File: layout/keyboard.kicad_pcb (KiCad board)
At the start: 2 copper layers, 281.5 x 105.2 mm, 127 parts, among them SW1 SW_PUSH, U1 ATMEGA32U4, X1 XTAL_GND

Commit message: switches layout
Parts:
- removed C1, C2, C3, C4, C5, C6, C7: 22pF, Capacitor_SMD:C_0805_2012Metric_Pad1.15x1.40mm_HandSolder
- removed D_A, D_ALT, D_B, D_BKSP, D_BSLSH, D_C, D_CBRAC, D_COMMA, D_CTRL, D_D, D_DOT, D_E, D_EQUAL, D_ESC, D_F, D_G, D_H, D_I, D_J, D_K, D_L, D_M, D_MINUS, D_N, D_O, D_OBRAC, D_P, D_Q, D_QUOTE, D_R, D_S, D_SEMIC, D_SHIFT, D_SLASH, D_SPACE, D_SUPER, D_T, D_TAB, D_U, D_V, D_W, D_X, D_Y, D_Z, D_`: D, keyboard_parts:D_SOD123_axial
- removed K_A, K_B, K_C, K_CBRAC, K_COMMA, K_D, K_DOT, K_E, K_EQUAL, K_ESC, K_F, K_G, K_H, K_I, K_J, K_K, K_L, K_M, K_MINUS, K_N, K_O, K_OBRAC, K_P, K_Q, K_QUOTE, K_R, K_S, K_SEMIC, K_SLASH, K_T, K_U, K_V, K_W, K_X, K_Y, K_Z, K_`: KEYSW, MX_Alps_Hybrid:MX-1U-NoLED
- removed K_ALT, K_SUPER: KEYSW, MX_Alps_Hybrid:MX-1.25U-NoLED
- removed K_BKSP: KEYSW, MX_Alps_Hybrid:MX-2U-NoLED
- removed K_BSLSH, K_TAB: KEYSW, MX_Alps_Hybrid:MX-1.5U-NoLED
- removed K_CTRL: KEYSW, MX_Alps_Hybrid:MX-1.75U-NoLED
- removed K_SHIFT, K_SPACE: KEYSW, MX_Alps_Hybrid:MX-2.25U-NoLED
- removed R1, R2: 10k, Resistor_SMD:R_0805_2012Metric_Pad1.15x1.40mm_HandSolder
- removed R3, R4: 22, Resistor_SMD:R_0805_2012Metric_Pad1.15x1.40mm_HandSolder
- removed SW1: SW_PUSH, Button_Switch_SMD:SW_SPST_TL3342
- removed USB1: Molex-0548190589, keyboard_parts:Molex-0548190589-Assembly
- removed X1: XTAL_GND, Crystal:Crystal_SMD_5032-4Pin_5.0x3.2mm
- added D_A1: D, keyboard_parts:D_SOD123_axial, F.Cu at (57.9, -65.9)
- added D_ALT1: D, keyboard_parts:D_SOD123_axial, F.Cu at (88.9, -27.8)
- added D_B1: D, keyboard_parts:D_SOD123_axial, F.Cu at (134.1, -46.8)
- added D_BKSP1: D, keyboard_parts:D_SOD123_axial, F.Cu at (258.0, -104.0)
- added D_BSLSH1: D, keyboard_parts:D_SOD123_axial, F.Cu at (253.2, -84.9)
- added D_C1: D, keyboard_parts:D_SOD123_axial, F.Cu at (96.0, -46.8)
- added D_CBRAC1: D, keyboard_parts:D_SOD123_axial, F.Cu at (234.2, -27.8)
- added D_COMMA1: D, keyboard_parts:D_SOD123_axial, F.Cu at (191.3, -47.1)
- added D_CTRL1: D, keyboard_parts:D_SOD123_axial, F.Cu at (31.8, -65.9)
- added D_D1: D, keyboard_parts:D_SOD123_axial, F.Cu at (134.1, -65.9)
- added D_DOT1: D, keyboard_parts:D_SOD123_axial, F.Cu at (210.3, -46.8)
- added D_E1: D, keyboard_parts:D_SOD123_axial, F.Cu at (191.3, -65.9)
- added D_EQUAL1: D, keyboard_parts:D_SOD123_axial, F.Cu at (215.1, -27.8)
- added D_ESC1: D, keyboard_parts:D_SOD123_axial, F.Cu at (38.9, -104.0)
- added D_F1: D, keyboard_parts:D_SOD123_axial, F.Cu at (96.0, -84.9)
- added D_G1: D, keyboard_parts:D_SOD123_axial, F.Cu at (134.1, -84.9)
- added D_H1: D, keyboard_parts:D_SOD123_axial, F.Cu at (153.2, -65.9)
- added D_I1: D, keyboard_parts:D_SOD123_axial, F.Cu at (210.3, -65.9)
- added D_J1: D, keyboard_parts:D_SOD123_axial, F.Cu at (153.2, -84.9)
- added D_K1: D, keyboard_parts:D_SOD123_axial, F.Cu at (153.2, -46.8)
- added D_L1: D, keyboard_parts:D_SOD123_axial, F.Cu at (172.2, -84.9)
- added D_M1: D, keyboard_parts:D_SOD123_axial, F.Cu at (172.2, -46.8)
- added D_MINUS1: D, keyboard_parts:D_SOD123_axial, F.Cu at (196.1, -27.8)
- added D_N1: D, keyboard_parts:D_SOD123_axial, F.Cu at (172.2, -65.9)
- added D_O1: D, keyboard_parts:D_SOD123_axial, F.Cu at (229.4, -65.9)
- added D_OBRAC1: D, keyboard_parts:D_SOD123_axial, F.Cu at (43.7, -27.8)
- added D_P1: D, keyboard_parts:D_SOD123_axial, F.Cu at (115.1, -84.9)
- added D_Q1: D, keyboard_parts:D_SOD123_axial, F.Cu at (57.9, -84.9)
- added D_QUOTE1: D, keyboard_parts:D_SOD123_axial, F.Cu at (248.4, -65.9)
- added D_R1: D, keyboard_parts:D_SOD123_axial, F.Cu at (77.0, -65.9)
- added D_S1: D, keyboard_parts:D_SOD123_axial, F.Cu at (96.0, -65.9)
- added D_SEMIC1: D, keyboard_parts:D_SOD123_axial, F.Cu at (229.4, -84.9)
- added D_SHIFT1: D, keyboard_parts:D_SOD123_axial, F.Cu at (27.0, -46.8)
- added D_SLASH1: D, keyboard_parts:D_SOD123_axial, F.Cu at (229.4, -46.8)
- added D_SPACE2: D, keyboard_parts:D_SOD123_axial, F.Cu at (165.1, -27.8)
- added D_SUPER1: D, keyboard_parts:D_SOD123_axial, F.Cu at (65.1, -27.8)
- added D_T1: D, keyboard_parts:D_SOD123_axial, F.Cu at (115.1, -65.9)
- added D_TAB1: D, keyboard_parts:D_SOD123_axial, F.Cu at (34.1, -84.9)
- added D_U1: D, keyboard_parts:D_SOD123_axial, F.Cu at (191.3, -84.9)
- added D_V1: D, keyboard_parts:D_SOD123_axial, F.Cu at (115.1, -46.8)
- added D_W1: D, keyboard_parts:D_SOD123_axial, F.Cu at (77.0, -84.9)
- added D_X1: D, keyboard_parts:D_SOD123_axial, F.Cu at (77.0, -46.8)
- added D_Y1: D, keyboard_parts:D_SOD123_axial, F.Cu at (210.3, -84.9)
- added D_Z1: D, keyboard_parts:D_SOD123_axial, F.Cu at (57.9, -46.8)
- added D_`1: D, keyboard_parts:D_SOD123_axial, F.Cu at (248.4, -46.8)
- added K_A1: KEYSW, MX_Only:MXOnly-1U-NoLED, F.Cu at (50.0, -65.9)
- added K_ALT1: KEYSW, MX_Only:MXOnly-1.25U-NoLED, F.Cu at (81.0, -27.8)
- added K_B1: KEYSW, MX_Only:MXOnly-1U-NoLED, F.Cu at (126.2, -46.8)
- added K_BKSP1: KEYSW, MX_Only:MXOnly-2U-NoLED, F.Cu at (250.0, -104.0)
- added K_BSLSH1: KEYSW, MX_Only:MXOnly-1.5U-NoLED, F.Cu at (245.3, -84.9)
- added K_C1: KEYSW, MX_Only:MXOnly-1U-NoLED, F.Cu at (88.1, -46.8)
- added K_CBRAC1: KEYSW, MX_Only:MXOnly-1U-NoLED, F.Cu at (226.2, -27.8)
- added K_COMMA1: KEYSW, MX_Only:MXOnly-1U-NoLED, F.Cu at (183.4, -46.8)
- added K_CTRL1: KEYSW, MX_Only:MXOnly-1.75U-NoLED, F.Cu at (23.8, -65.9)
- added K_D1: KEYSW, MX_Only:MXOnly-1U-NoLED, F.Cu at (126.2, -65.9)
- added K_DOT1: KEYSW, MX_Only:MXOnly-1U-NoLED, F.Cu at (202.4, -46.8)
- added K_E1: KEYSW, MX_Only:MXOnly-1U-NoLED, F.Cu at (183.4, -65.9)
- added K_EQUAL1: KEYSW, MX_Only:MXOnly-1U-NoLED, F.Cu at (207.2, -27.8)
- added K_ESC1: KEYSW, MX_Only:MXOnly-1U-NoLED, F.Cu at (31.0, -104.0)
- added K_F1: KEYSW, MX_Only:MXOnly-1U-NoLED, F.Cu at (88.1, -84.9)
- added K_G1: KEYSW, MX_Only:MXOnly-1U-NoLED, F.Cu at (126.2, -84.9)
- added K_H1: KEYSW, MX_Only:MXOnly-1U-NoLED, F.Cu at (145.3, -65.9)
- added K_I1: KEYSW, MX_Only:MXOnly-1U-NoLED, F.Cu at (202.4, -65.9)
- added K_J1: KEYSW, MX_Only:MXOnly-1U-NoLED, F.Cu at (145.3, -84.9)
- added K_K1: KEYSW, MX_Only:MXOnly-1U-NoLED, F.Cu at (145.3, -46.8)
- added K_L1: KEYSW, MX_Only:MXOnly-1U-NoLED, F.Cu at (164.3, -84.9)
- added K_M1: KEYSW, MX_Only:MXOnly-1U-NoLED, F.Cu at (164.3, -46.8)
- added K_MINUS1: KEYSW, MX_Only:MXOnly-1U-NoLED, F.Cu at (188.1, -27.8)
- added K_N1: KEYSW, MX_Only:MXOnly-1U-NoLED, F.Cu at (164.3, -65.9)
- added K_O1: KEYSW, MX_Only:MXOnly-1U-NoLED, F.Cu at (221.5, -65.9)
- added K_OBRAC1: KEYSW, MX_Only:MXOnly-1U-NoLED, F.Cu at (35.7, -27.8)
- added K_P1: KEYSW, MX_Only:MXOnly-1U-NoLED, F.Cu at (107.2, -84.9)
- added K_Q1: KEYSW, MX_Only:MXOnly-1U-NoLED, F.Cu at (50.0, -84.9)
- added K_QUOTE1: KEYSW, MX_Only:MXOnly-1U-NoLED, F.Cu at (240.5, -65.9)
- added K_R1: KEYSW, MX_Only:MXOnly-1U-NoLED, F.Cu at (69.1, -65.9)
- added K_S1: KEYSW, MX_Only:MXOnly-1U-NoLED, F.Cu at (88.1, -65.9)
- added K_SEMIC1: KEYSW, MX_Only:MXOnly-1U-NoLED, F.Cu at (221.5, -84.9)
- added K_SHIFT1: KEYSW, MX_Only:MXOnly-2.25U-NoLED, F.Cu at (19.1, -46.8)
- added K_SLASH1: KEYSW, MX_Only:MXOnly-1U-NoLED, F.Cu at (221.5, -46.8)
- added K_SPACE2: KEYSW, MX_Only:MXOnly-2.25U-NoLED, F.Cu at (157.2, -27.8)
- added K_SUPER1: KEYSW, MX_Only:MXOnly-1.25U-NoLED, F.Cu at (57.1, -27.8)
- added K_T1: KEYSW, MX_Only:MXOnly-1U-NoLED, F.Cu at (107.2, -65.9)
- added K_TAB1: KEYSW, MX_Only:MXOnly-1.5U-NoLED, F.Cu at (26.2, -84.9)
- added K_U1: KEYSW, MX_Only:MXOnly-1U-NoLED, F.Cu at (183.4, -84.9)
- added K_V1: KEYSW, MX_Only:MXOnly-1U-NoLED, F.Cu at (107.2, -46.8)
- added K_W1: KEYSW, MX_Only:MXOnly-1U-NoLED, F.Cu at (69.1, -84.9)
- added K_X1: KEYSW, MX_Only:MXOnly-1U-NoLED, F.Cu at (69.1, -46.8)
- added K_Y1: KEYSW, MX_Only:MXOnly-1U-NoLED, F.Cu at (202.4, -84.9)
- added K_Z1: KEYSW, MX_Only:MXOnly-1U-NoLED, F.Cu at (50.0, -46.8)
- added K_`1: KEYSW, MX_Only:MXOnly-1U-NoLED, F.Cu at (240.5, -46.8)
- K_0, K_1, K_2, K_3, K_4, K_5, K_6, K_7, K_8, K_9: footprint MX_Alps_Hybrid:MX-1U-NoLED -> MX_Only:MXOnly-1U-NoLED
- K_SPACE1: footprint MX_Alps_Hybrid:MX-2.25U-NoLED -> MX_Only:MXOnly-2.25U-NoLED
- U1: value ATMEGA32U4 -> ProMicro; footprint Package_QFP:TQFP-44_10x10mm_P0.8mm -> Keebio-Parts:ArduinoProMicro; moved to F.Cu
- moved U1 297.5 mm to (10.3, -95.2), turned to 270 degrees
- moved D_SPACE1 128.4 mm to (122.2, -27.7)
- moved K_SPACE1 122.2 mm to (114.3, -27.8)
- moved D_0 114.1 mm to (229.4, -104.0)
- moved D_1 114.1 mm to (57.9, -104.0)
- moved D_2 114.1 mm to (77.0, -104.0)
- moved D_3 114.1 mm to (96.0, -104.0)
- moved D_4 114.1 mm to (115.1, -104.0)
- moved D_5 114.1 mm to (134.1, -104.0)
- moved D_6 114.1 mm to (153.2, -104.0)
- moved D_7 114.1 mm to (172.2, -104.0)
- moved D_8 114.1 mm to (191.3, -104.0)
- moved D_9 114.1 mm to (210.3, -104.0)
- moved K_0 113.5 mm to (221.5, -104.0)
- moved K_1 113.5 mm to (50.0, -104.0)
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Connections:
- D_0 pad 1: /row0 -> row0
- D_1 pad 1: /row0 -> row0
- D_2 pad 1: /row0 -> row0
- D_3 pad 1: /row0 -> row0
- D_4 pad 1: /row0 -> row0
- D_5 pad 1: /row0 -> row0
- D_6 pad 1: /row0 -> row0
- D_7 pad 1: /row0 -> row0
- D_8 pad 1: /row0 -> row0
- D_9 pad 1: /row0 -> row0
- D_SPACE1 pad 1: /row4 -> row4
- K_0 pad 1: /col10 -> col10
- K_1 pad 1: /col1 -> col1
- K_2 pad 1: /col2 -> col2
- K_3 pad 1: /col3 -> col3
- K_4 pad 1: /col4 -> col4
- K_5 pad 1: /col5 -> col5
- K_6 pad 1: /col6 -> col6
- K_7 pad 1: /col7 -> col7
- K_8 pad 1: /col8 -> col8
- K_9 pad 1: /col9 -> col9
- K_SPACE1 pad 1: /col7 -> col7
- U1 pad 1: Net-(U1-Pad1) -> row4
- U1 pad 10: /row2 -> col5
- U1 pad 11: /row3 -> col6
- U1 pad 12: /col2 -> col7
- U1 pad 13: Net-(R1-Pad1) -> col8
- U1 pad 14: VCC -> col9
- U1 pad 15: GND -> col10
- U1 pad 16: Net-(C1-Pad1) -> col11
- U1 pad 17: Net-(C2-Pad1) -> row0
- U1 pad 18: /col5 -> row1
- U1 pad 19: /col6 -> row2
- U1 pad 2: VCC -> Net-(U1-Pad2)
- U1 pad 20: /col7 -> row3
- U1 pad 21: /col8 -> Net-(U1-Pad21)
- U1 pad 22: /col10 -> Net-(U1-Pad22)
- U1 pad 23: GND -> +5V
- U1 pad 24: VCC -> Net-(U1-Pad24)
- U1 pad 5: GND -> col0
- U1 pad 6: Net-(C3-Pad1) -> col1
- U1 pad 7: Net-(U1-Pad7) -> col2
- U1 pad 8: /row0 -> col3
- U1 pad 9: /row1 -> col4

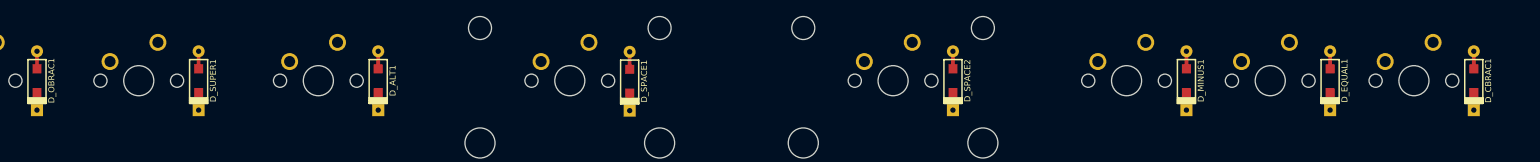
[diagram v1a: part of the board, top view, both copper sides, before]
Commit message: unswitching cols
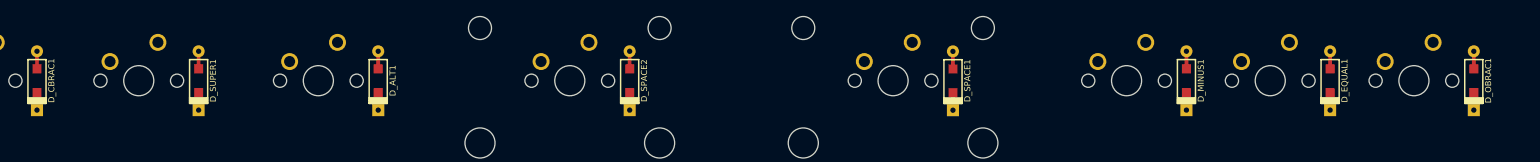
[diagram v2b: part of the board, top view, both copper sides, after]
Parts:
- moved D_CBRAC1 190.5 mm to (43.7, -27.8)
- moved D_OBRAC1 190.5 mm to (234.2, -27.8)
- moved K_CBRAC1 190.5 mm to (35.7, -27.8)
- moved K_OBRAC1 190.5 mm to (226.2, -27.8)
- moved D_SPACE1 42.9 mm to (165.1, -27.8)
- moved D_SPACE2 42.9 mm to (122.2, -27.8)
- moved K_SPACE1 42.9 mm to (157.2, -27.8)
- moved K_SPACE2 42.9 mm to (114.3, -27.8)

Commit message: routing to pro micro
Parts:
- moved D_EQUAL1 167.9 mm to (276.2, 128.6)
- moved K_EQUAL1 167.9 mm to (268.3, 128.6)
- moved D_0 167.9 mm to (290.5, 52.4)
- moved D_1 167.9 mm to (119.1, 52.4)
- moved D_2 167.9 mm to (138.1, 52.4)
- moved D_3 167.9 mm to (157.2, 52.4)
- moved D_4 167.9 mm to (176.2, 52.4)
- moved D_5 167.9 mm to (195.3, 52.4)
- moved D_6 167.9 mm to (214.3, 52.4)
- moved D_7 167.9 mm to (233.4, 52.4)
- moved D_8 167.9 mm to (252.4, 52.4)
- moved D_9 167.9 mm to (271.5, 52.4)
- moved D_ALT1 167.9 mm to (150.0, 128.6)
- moved D_BKSP1 167.9 mm to (319.1, 52.4)
- moved D_BSLSH1 167.9 mm to (314.3, 71.4)
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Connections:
- U1 pad 1: row4 -> col5
- U1 pad 10: col5 -> row2
- U1 pad 11: col6 -> row3
- U1 pad 12: col7 -> row4
- U1 pad 13: col8 -> col11
- U1 pad 14: col9 -> col10
- U1 pad 15: col10 -> col9
- U1 pad 16: col11 -> col8
- U1 pad 17: row0 -> col7
- U1 pad 18: row1 -> col6
- U1 pad 19: row2 -> row1
- U1 pad 20: row3 -> row0
- U1 pad 5: col0 -> col4
- U1 pad 6: col1 -> col3
- U1 pad 8: col3 -> col1
- U1 pad 9: col4 -> col0
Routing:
- net col11: track 0.00 -> 306.8 mm, vias 0 -> 1
- net col10: track 0.00 -> 288.4 mm, vias 0 -> 1
- net row3: track 0.00 -> 279.3 mm
- net col9: track 0.00 -> 273.5 mm, vias 0 -> 1
- net row4: track 0.00 -> 271.3 mm
- net row2: track 0.00 -> 260.4 mm
- net col7: track 0.00 -> 252.1 mm, vias 0 -> 1
- net row1: track 0.00 -> 242.9 mm
- net row0: track 0.00 -> 240.7 mm
- net col8: track 0.00 -> 233.2 mm, vias 0 -> 1
- net col5: track 0.00 -> 226.9 mm, vias 0 -> 1
- net col6: track 0.00 -> 202.6 mm, vias 0 -> 1
- net col3: track 0.00 -> 175.6 mm, vias 0 -> 1
- net col4: track 0.00 -> 174.5 mm, vias 0 -> 1
- net col2: track 0.00 -> 156.6 mm, vias 0 -> 1
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- removed copper zone on B.Cu, net GND
- removed copper zone on F.Cu, net VCC
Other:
- board outline removed
- board text removed: "PCB Builder by MisterKeebs - mrkeebs.com"

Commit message: egdes, and flip diodes to back
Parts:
- D_0, D_1, D_2, D_3, D_4, D_5, D_6, D_7, D_8, D_9, D_A1, D_ALT1, D_B1, D_BKSP1, D_BSLSH1, D_C1, D_CBRAC1, D_COMMA1, D_CTRL1, D_D1, D_DOT1, D_E1, D_EQUAL1, D_ESC1, D_F1, D_G1, D_H1, D_I1, D_J1, D_K1, D_L1, D_M1, D_MINUS1, D_N1, D_O1, D_OBRAC1, D_P1, D_Q1, D_QUOTE1, D_R1, D_S1, D_SEMIC1, D_SHIFT1, D_SLASH1, D_SPACE1, D_SPACE2, D_SUPER1, D_T1, D_TAB1, D_U1, D_V1, D_W1, D_X1, D_Y1, D_Z1, D_`1: moved to B.Cu
- K_SPACE1, K_SPACE2: footprint MX_Only:MXOnly-2.25U-NoLED -> MX_Only:MXOnly-2.25U-ReversedStabilizers-NoLED
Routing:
- net Net-(D_SPACE1-Pad2): track 0.00 -> 5.89 mm
- net Net-(D_S1-Pad2): track 0.00 -> 5.89 mm
- net Net-(D_P1-Pad2): track 0.00 -> 5.89 mm
- net Net-(D_J1-Pad2): track 0.00 -> 5.89 mm
- net Net-(D_W1-Pad2): track 0.00 -> 5.89 mm
- net Net-(D_SLASH1-Pad2): track 0.00 -> 5.89 mm
- net Net-(D_D1-Pad2): track 0.00 -> 5.89 mm
- net Net-(D_EQUAL1-Pad2): track 0.00 -> 5.89 mm
- net Net-(D_X1-Pad2): track 0.00 -> 5.89 mm
- net Net-(D_V1-Pad2): track 0.00 -> 5.89 mm
- net Net-(D_T1-Pad2): track 0.00 -> 5.89 mm
- net Net-(D_SHIFT1-Pad2): track 0.00 -> 5.89 mm
- net Net-(D_R1-Pad2): track 0.00 -> 5.89 mm
- net Net-(D_N1-Pad2): track 0.00 -> 5.89 mm
- net Net-(D_MINUS1-Pad2): track 0.00 -> 5.89 mm
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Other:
- board outline added: 271.5 x 95.3 mm
